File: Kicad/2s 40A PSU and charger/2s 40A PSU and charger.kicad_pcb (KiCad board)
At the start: 4 copper layers, 44.9 x 42 mm, 133 parts, among them J1 JST SH SM04B/Qwiic, J2 7 pin FPC 0.3mm Panasonic Y3b, J3 Conn_01x03, J4 Conn_01x03, J5 JST XH-S, Q1 PJA3430, Q2 PJA3430, Q3 Vishay sir404dp, Q4 PJA3430, Q5 PJA3430, Q7 Vishay sir404dp, SW1 KMR2, SW2 KMR2, U2 AP63203WU, U3 BQ76905RGRR, U4 BQ24780SRUYR, U5 ESP32-S3, U6 74HC595, Y1 40mhz, 10ppm

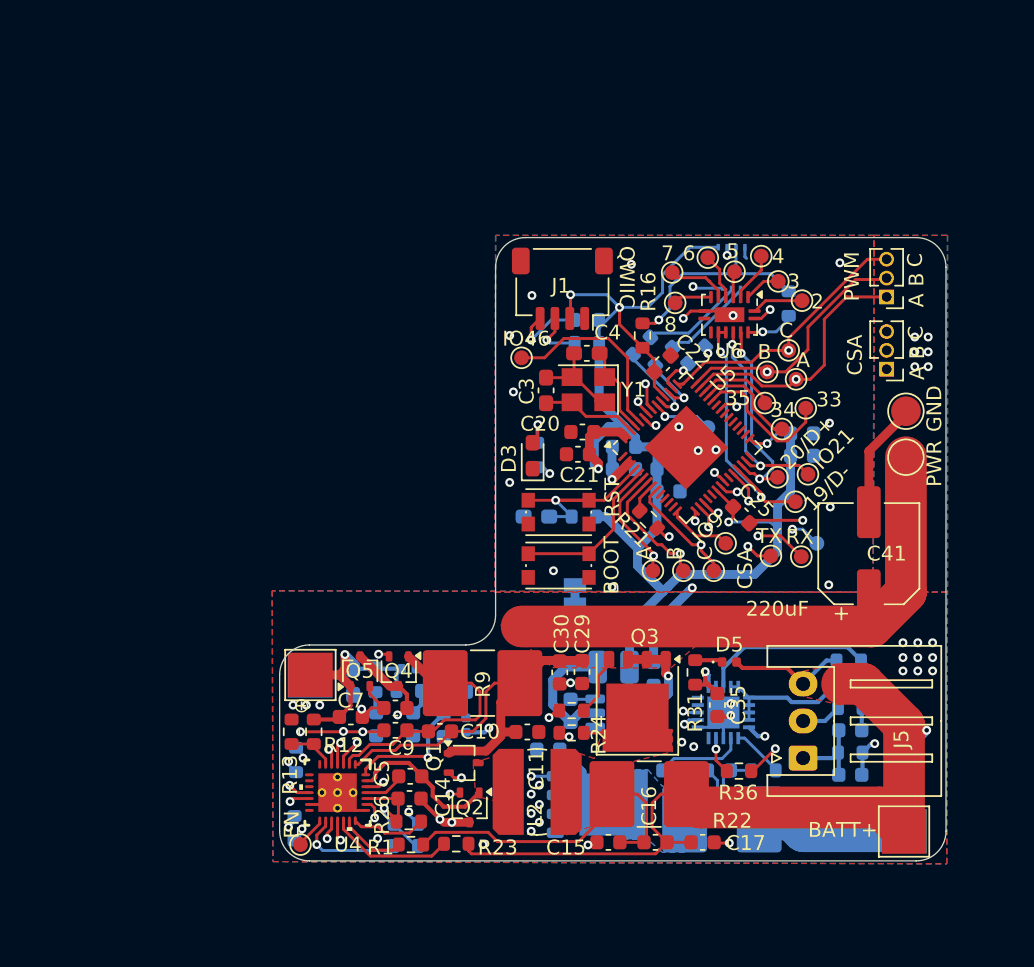
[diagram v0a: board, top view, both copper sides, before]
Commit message: Rearranged schematic hierarchy
It should be clearer than the original design from my testing board. I haven't changed any of the design things except getting the correct small transistor footprint (errata from before)
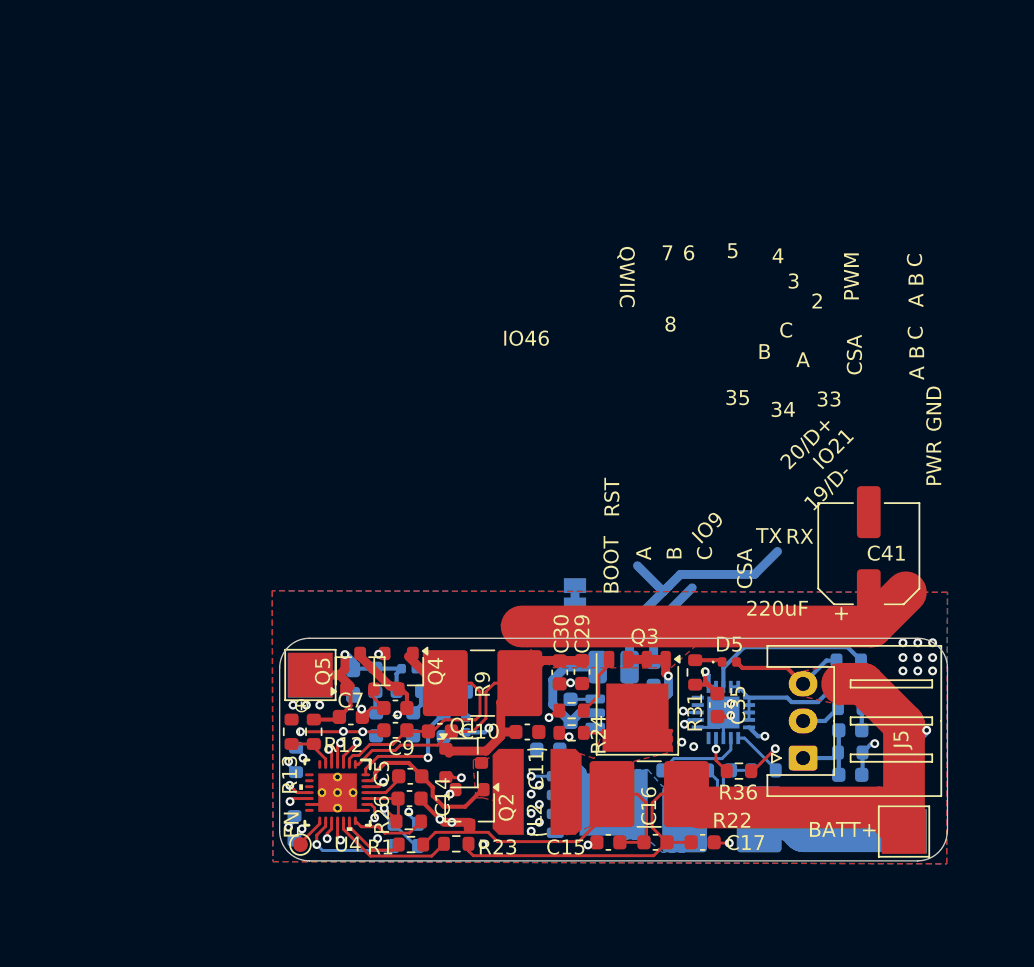
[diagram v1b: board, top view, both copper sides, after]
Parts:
- removed C1, C2, C21, C24: 1uF, Capacitor_SMD:C_0603_1608Metric
- removed C18: 1uF, Capacitor_SMD:C_0603_1608Metric_Pad1.08x0.95mm_HandSolder
- removed C19, C20, C22, C23, C25: 0.1uF, Capacitor_SMD:C_0603_1608Metric
- removed C26: 22uF, Capacitor_SMD:C_0603_1608Metric
- removed C3, C4: 16pF, Capacitor_SMD:C_0603_1608Metric_Pad1.08x0.95mm_HandSolder
- removed D3: Osram LT Q99G.01 green led, LED_SMD:LED_0603_1608Metric_Pad1.05x0.95mm_HandSolder
- removed FB1: 120ohm imp @100mhz, Inductor_SMD:L_0603_1608Metric
- removed H5: GND, TestPoint:TestPoint_Pad_D2.0mm
- removed H6: Power, TestPoint:TestPoint_Pad_D2.0mm
- removed J1: JST SH SM04B/Qwiic, Connector_JST:JST_SH_SM04B-SRSS-TB_1x04-1MP_P1.00mm_Horizontal
- removed J2: 7 pin FPC 0.3mm Panasonic Y3b, custom_Interface_HID:fpc_7pin_0.3mm_connector Panasonic
- removed J3, J4: Conn_01x03, Connector_PinHeader_1.27mm:PinHeader_1x03_P1.27mm_Vertical
- removed R14, R15, R16, R20: 10k, Resistor_SMD:R_0603_1608Metric
- removed R19: 80.6 ohm, Resistor_SMD:R_0603_1608Metric
- removed R21: 100k, Resistor_SMD:R_0603_1608Metric
- removed R3, R4, R5, R6: 33ohm, Resistor_SMD:R_0603_1608Metric
- removed SW1, SW2: KMR2, Button_Switch_SMD:SW_Push_1P1T_NO_CK_KMR2
- removed TP1, TP14, TP15: TestPoint, TestPoint:TestPoint_Pad_D1.0mm
- removed TP10, TP11, TP12, TP18, TP19, TP2, TP20, TP21, TP22, TP24, TP25, TP26, TP27, TP28, TP29, TP3, TP30, TP4, TP5, TP7, TP8, TP9: ~, TestPoint:TestPoint_Pad_D1.0mm
- removed U5: ESP32-S3, Package_DFN_QFN:QFN-56-1EP_7x7mm_P0.4mm_EP4x4mm
- removed U6: 74HC595, Package_DFN_QFN:DHVQFN-16-1EP_2.5x3.5mm_P0.5mm_EP1x2mm
- removed Y1: 40mhz, 10ppm, Crystal:Crystal_SMD_3225-4Pin_3.2x2.5mm
- Q1, Q2, Q4, Q5: footprint Package_TO_SOT_SMD:SOT-323_SC-70 -> Package_TO_SOT_SMD:SC-59
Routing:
- net VDD: track 108.8 -> 21.8 mm, vias 6 -> 0
- net /1CSA-A: track 36.1 -> 0.00 mm, vias 1 -> 0
- net /1CSA-B: track 35.7 -> 0.00 mm, vias 1 -> 0
- net /1CSA-C: track 33.3 -> 0.00 mm, vias 1 -> 0
- net /1A: track 28.2 -> 0.00 mm, vias 2 -> 0
- net /1B: track 26.3 -> 0.00 mm, vias 2 -> 0
- net /SCL1: track 78.5 -> 52.3 mm, vias 5 -> 3
- net /1C: track 25.6 -> 0.00 mm, vias 2 -> 0
- net /SDA1: track 72.3 -> 49.7 mm, vias 5 -> 3
- net /UART0_TX: track 19.9 -> 0.00 mm, vias 2 -> 0
- net Net-(U5-GPIO19/USB_D-): track 17.8 -> 0.00 mm, vias 2 -> 0
- net /UART0_RX: track 17.5 -> 0.00 mm, vias 2 -> 0
- net GND: track 22.6 -> 6.10 mm, vias 20 -> 0
- net /CS1: track 14.5 -> 0.00 mm, vias 1 -> 0
- net Net-(U5-GPIO21): track 14.4 -> 0.00 mm, vias 2 -> 0
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- removed copper zone on B.Cu, net GND
- removed copper zone on F.Cu, net GND
- removed copper zone on In1.Cu, net GND
- removed copper zone on In2.Cu, net GND
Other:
- board size 44.9 x 42 mm -> 45 x 15 mm
- rule pad_to_mask_clearance: 0 -> 0.05

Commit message: Reworked PSU to use CH32X035 and USB-PD
This will save a few bucks and will actually be a cooler solution than just a DC jack connected to some pads
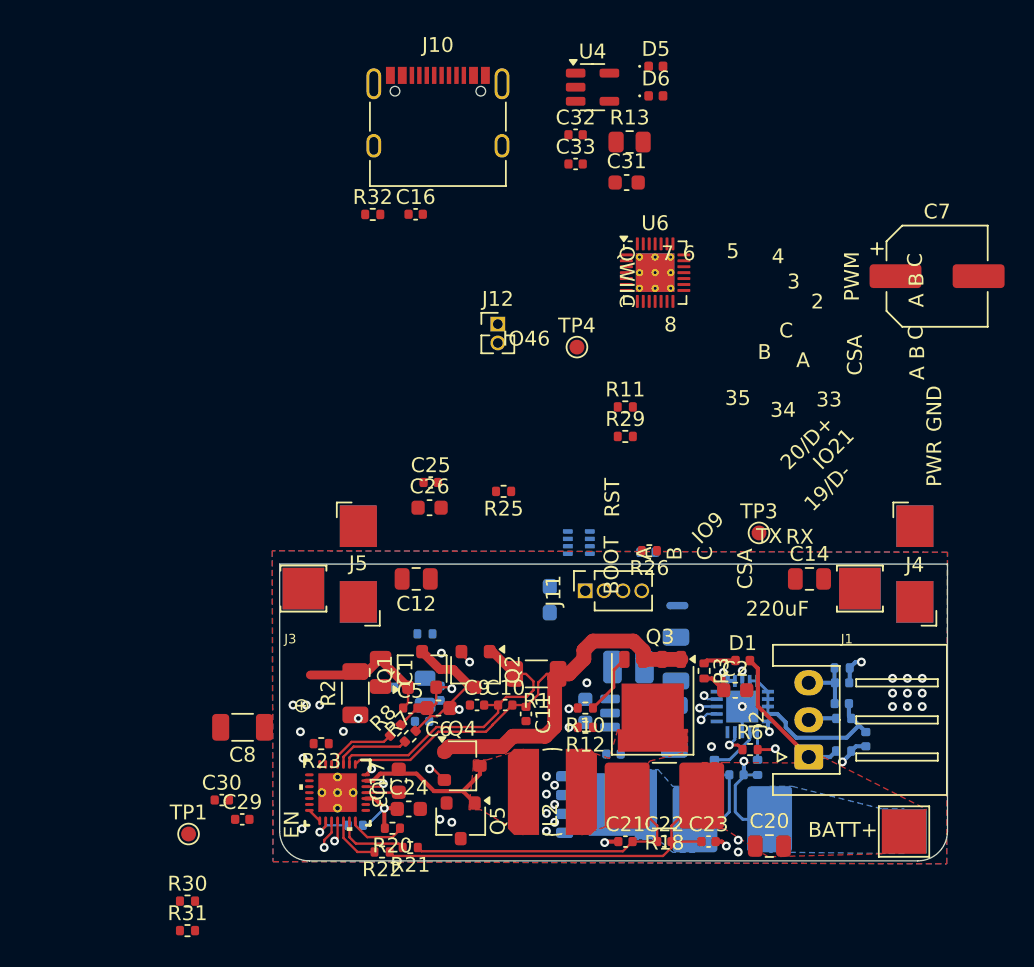
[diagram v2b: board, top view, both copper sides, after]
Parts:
- removed C34: 22nF, Capacitor_SMD:C_0603_1608Metric
- removed C35: 2.2uf, Capacitor_SMD:C_0603_1608Metric
- removed C36: 10uF, Capacitor_SMD:C_0603_1608Metric
- removed C37, C39: 220nF, Capacitor_SMD:C_0603_1608Metric
- removed C38: 0.1uF, Capacitor_SMD:C_0603_1608Metric
- removed C41: 220uF,APA0609221M016R, Capacitor_SMD:CP_Elec_6.3x9.9
- removed H3, H4: Pad, TestPoint:TestPoint_Pad_3.0x3.0mm
- removed L1: GND joiner, Jumper:SolderJumper-2_P1.3mm_Bridged_Pad1.0x1.5mm
- removed Q7: Vishay sir404dp, Package_DFN_QFN:PQFN-8-EP_6x5mm_P1.27mm_Generic
- removed R33, R34, R35: 10ohm, Resistor_SMD:R_0603_1608Metric
- removed R36: 5.1k, Resistor_SMD:R_0603_1608Metric
- removed TP6: ~, TestPoint:TestPoint_Pad_D1.0mm
- added C1: 10uF, 16v, Capacitor_SMD:C_0805_2012Metric, F.Cu at (114.9, 119.3)
- added C18: 220nF, 16v, Capacitor_SMD:C_0402_1005Metric, B.Cu at (146.0, 121.4)
- added C19: 220nF, 16v, Capacitor_SMD:C_0402_1005Metric, B.Cu at (146.0, 120.0)
- added C2: 2.2uf, 16v, Capacitor_SMD:C_0603_1608Metric, F.Cu at (138.8, 120.5)
- added C20: 10uF, 16v, Capacitor_SMD:C_0805_2012Metric, F.Cu at (141.1, 131.0)
- added C21: 0.1uF, 16v, Capacitor_SMD:C_0402_1005Metric, F.Cu at (131.4, 130.7)
- added C22: 0.1uF, 16v, Capacitor_SMD:C_0402_1005Metric, F.Cu at (134.0, 130.7)
- added C23: 0.1uF, 16v, Capacitor_SMD:C_0402_1005Metric, F.Cu at (137.0, 130.7)
- added C24: 2.2uf, Capacitor_SMD:C_0603_1608Metric, F.Cu at (116.8, 128.5)
- added C25: 0.1uF, Capacitor_SMD:C_0402_1005Metric, F.Cu at (118.3, 106.5)
- added C26: 4.7uF, Capacitor_SMD:C_0603_1608Metric, F.Cu at (118.2, 108.2)
- added C3: 0.1uF, 16v, Capacitor_SMD:C_0402_1005Metric, B.Cu at (138.9, 126.2)
- added C32: 0.1uF, 16v, Capacitor_SMD:C_0402_1005Metric, F.Cu at (128.0, 83.1)
- added C4: 0.1uF, Capacitor_SMD:C_0402_1005Metric, B.Cu at (130.6, 124.8)
- added D1: GSDH3005, Diode_SMD:D_0402_1005Metric, F.Cu at (139.3, 118.5)
- added D3: GSDH3005, Diode_SMD:D_0402_1005Metric, B.Cu at (118.9, 120.7)
- added D6: GSDH3005, Diode_SMD:D_0402_1005Metric, F.Cu at (133.4, 80.5)
- added J1: Keystone 3579, custom_Connector:Keystone_3579, F.Cu at (147.2, 113.7)
- added J10: USB_C_Receptacle_USB2.0_16P, Connector_USB:USB_C_Receptacle_XKB_U262-16XN-4BVC11, F.Cu at (118.8, 82.7)
- added J11: 1.27mm 4 pin socket, Connector_PinSocket_1.27mm:PinSocket_1x04_P1.27mm_Vertical, F.Cu at (128.7, 113.8)
- added J12: USB, Connector_PinHeader_1.27mm:PinHeader_1x02_P1.27mm_Vertical, F.Cu at (122.8, 95.8)
- added J2: JST XH-S, Connector_JST:JST_XH_S3B-XH-A_1x03_P2.50mm_Horizontal, F.Cu at (143.8, 125.0)
- added J3: Keystone 3579, custom_Connector:Keystone_3579, F.Cu at (109.7, 113.7)
- added J4: Keystone 3569, custom_Connector:Keystone_3569, F.Cu at (150.9, 112.0)
- added J6: Keystone 3579, custom_Connector:Keystone_3579, B.Cu at (147.2, 113.7)
- added J7: Keystone 3579, custom_Connector:Keystone_3579, B.Cu at (109.7, 113.7)
- added J8: Keystone 3569, custom_Connector:Keystone_3569, B.Cu at (150.9, 112.0)
- added J9: Keystone 3569, custom_Connector:Keystone_3569, B.Cu at (113.4, 112.0)
- added NT1: NetTie_2, NetTie:NetTie-2_SMD_Pad0.5mm, B.Cu at (134.9, 114.8)
- added Q6: Vishay sir404dp, or SiR500DP, Package_DFN_QFN:PQFN-8-EP_6x5mm_P1.27mm_Generic, B.Cu at (130.0, 128.2)
- added R14: 1mOhm, CS wshp2818, Resistor_SMD:R_2816_7142Metric, B.Cu at (138.6, 129.2)
- added R15: 10ohm, Resistor_SMD:R_0402_1005Metric, B.Cu at (146.1, 124.6)
- added R16: 10ohm, Resistor_SMD:R_0402_1005Metric, B.Cu at (146.1, 122.4)
- added R17: 10ohm, Resistor_SMD:R_0402_1005Metric, B.Cu at (146.0, 119.0)
- added R20: 10k, Resistor_SMD:R_0402_1005Metric, F.Cu at (115.7, 129.8)
- added R21: 10ohm, Resistor_SMD:R_0402_1005Metric, F.Cu at (116.9, 131.1)
- added R3: 100ohm, Resistor_SMD:R_0402_1005Metric, F.Cu at (136.7, 119.2)
- added R32: 100k, Resistor_SMD:R_0402_1005Metric, F.Cu at (114.4, 88.4)
- added R4: 100ohm, Resistor_SMD:R_0402_1005Metric, B.Cu at (140.3, 125.7)
- added R5: 100ohm, Resistor_SMD:R_0402_1005Metric, B.Cu at (137.4, 125.7)
- added R6: 5.1k, Resistor_SMD:R_0402_1005Metric, F.Cu at (139.8, 124.5)
- added TP1: SWC, TestPoint:TestPoint_Pad_D1.0mm, F.Cu at (102.0, 130.2)
- added TP3: ~, TestPoint:TestPoint_Pad_D1.0mm, F.Cu at (140.4, 109.9)
- added TP4: SWD, TestPoint:TestPoint_Pad_D1.0mm, F.Cu at (128.1, 97.4)
- added U1: BQ76905RGRR, BQ76905:VQFN20_RGR_TEX, B.Cu at (139.3, 121.6)
- added U5: THVD1420DRLR, Package_TO_SOT_SMD:SOT-583-8, B.Cu at (128.3, 110.5)
- added U6: CH32X035G8U6, Package_DFN_QFN:QFN-28-1EP_4x4mm_P0.4mm_EP2.6x2.6mm_ThermalVias, F.Cu at (133.4, 92.4)
- C10, C11, C9: value 0.1uF -> 0.1uF, 16v; footprint Capacitor_SMD:C_0603_1608Metric -> Capacitor_SMD:C_0402_1005Metric
- C12: value 1uf -> 10uF, 16v; footprint Capacitor_SMD:C_0603_1608Metric -> Capacitor_SMD:C_0805_2012Metric; moved to F.Cu
- C13: value 10uF, 16v -> 220nF, 16v; footprint Capacitor_SMD:C_0603_1608Metric_Pad1.08x0.95mm_HandSolder -> Capacitor_SMD:C_0402_1005Metric
- C14: value 2.2uf -> 10uF, 16v; footprint Capacitor_SMD:C_0603_1608Metric -> Capacitor_SMD:C_0805_2012Metric
- C15: value 0.1uF -> 1uf, 16v; footprint Capacitor_SMD:C_0603_1608Metric -> Capacitor_SMD:C_0402_1005Metric; moved to B.Cu
- C16: value 0.1uF -> 100nF; footprint Capacitor_SMD:C_0603_1608Metric -> Capacitor_SMD:C_0402_1005Metric
- C17: value 0.1uF -> 47nF, 16v
- C27, C28: value 22uf -> 22uf, 16v CL31A226MOCLNN; footprint Capacitor_SMD:C_0603_1608Metric -> Capacitor_SMD:C_1206_3216Metric
- C29, C30: value 10uF -> 100pF; footprint Capacitor_SMD:C_0603_1608Metric -> Capacitor_SMD:C_0402_1005Metric
- C31: value 2.2uf -> 10uF, 16v; moved to F.Cu
- C33: value 0.1uF -> 2.2uF, 10v; footprint Capacitor_SMD:C_0603_1608Metric -> Capacitor_SMD:C_0402_1005Metric; moved to F.Cu
- C5: value 47nF -> 1nF; footprint Capacitor_SMD:C_0603_1608Metric -> Capacitor_SMD:C_0402_1005Metric
- C6: value 2.2uf -> 47nf; moved to F.Cu
- C7: value 1nF -> 220uF,APA0609221M016R; footprint Capacitor_SMD:C_0603_1608Metric -> Capacitor_SMD:CP_Elec_6.3x9.9
- C8: value 47nf -> 2.2uf, 16v; footprint Capacitor_SMD:C_0603_1608Metric -> Capacitor_SMD:C_1206_3216Metric
- D4: value GSDH3005 -> Osram LT Q99G.01 green led; footprint Diode_SMD:D_0402_1005Metric -> LED_SMD:LED_0603_1608Metric_Pad1.05x0.95mm_HandSolder
- J5: value JST XH-S -> Keystone 3569; footprint Connector_JST:JST_XH_S3B-XH-A_1x03_P2.50mm_Horizontal -> custom_Connector:Keystone_3569
- L2: value 5.6uH Bourns SDE0604A -> 6.8uH HPC HPC5040NF-6R8M
- L3: value 4.7uH, MAMK2520T4R7M -> 2.2uH, WIP322512A-2R2MLDG
- Q3: value Vishay sir404dp -> Vishay sir404dp, or SiR500DP
- R1: value 10ohm -> 10mOhm LVT12R0100FER; footprint Resistor_SMD:R_0603_1608Metric -> Resistor_SMD:R_1206_3216Metric
- R10: value 10k -> 4.02kohm; footprint Resistor_SMD:R_0603_1608Metric -> Resistor_SMD:R_0402_1005Metric; moved to F.Cu
- R11: value 2ohm -> 10k; footprint Resistor_SMD:R_0603_1608Metric -> Resistor_SMD:R_0402_1005Metric; moved to F.Cu
- R12: value 866k -> 10ohm; footprint Resistor_SMD:R_0603_1608Metric -> Resistor_SMD:R_0402_1005Metric
- R13: value 133k -> 10 ohm; footprint Resistor_SMD:R_0603_1608Metric -> Resistor_SMD:R_0805_2012Metric
- R18: value 10k -> 5mOhm, CS wshp2818; footprint Resistor_SMD:R_0603_1608Metric -> Resistor_SMD:R_2816_7142Metric; moved to F.Cu
- R2: value 4.02k -> 2ohm; footprint Resistor_SMD:R_0603_1608Metric -> Resistor_SMD:R_1206_3216Metric; moved to F.Cu
- R22: value 5mOhm, CS wshp2818 -> 10ohm; footprint Resistor_SMD:R_2816_7142Metric -> Resistor_SMD:R_0402_1005Metric
- R23: value 10ohm -> 10k; footprint Resistor_SMD:R_0603_1608Metric -> Resistor_SMD:R_0402_1005Metric
- R24: value 10ohm -> 10k; footprint Resistor_SMD:R_0603_1608Metric -> Resistor_SMD:R_0402_1005Metric; moved to B.Cu
- R25: value 4.02kohm -> 80.6 ohm; footprint Resistor_SMD:R_0603_1608Metric -> Resistor_SMD:R_0402_1005Metric
- R26: value 10k -> 120 ohm; footprint Resistor_SMD:R_0603_1608Metric -> Resistor_SMD:R_0402_1005Metric
- R27: value 1mOhm, CS wshp2818 -> 120 ohm; footprint Resistor_SMD:R_2816_7142Metric -> Resistor_SMD:R_0402_1005Metric
- R28: value 2ohm -> 120 ohm; footprint Resistor_SMD:R_0603_1608Metric -> Resistor_SMD:R_0402_1005Metric
- R29: value 100ohm -> 10k; footprint Resistor_SMD:R_0603_1608Metric -> Resistor_SMD:R_0402_1005Metric; moved to F.Cu
- R30: value 100ohm -> 866k; footprint Resistor_SMD:R_0603_1608Metric -> Resistor_SMD:R_0402_1005Metric; moved to F.Cu
- R31: value 10k -> 866k; footprint Resistor_SMD:R_0603_1608Metric -> Resistor_SMD:R_0402_1005Metric
- R7: footprint Resistor_SMD:R_0603_1608Metric -> Resistor_SMD:R_0402_1005Metric; moved to F.Cu
- R8: value 10k -> 4.02k; footprint Resistor_SMD:R_0603_1608Metric -> Resistor_SMD:R_0402_1005Metric; moved to F.Cu
- R9: value 5mOhm CS wshp2818 -> 10 ohm; footprint Resistor_SMD:R_2816_7142Metric -> Resistor_SMD:R_0805_2012Metric; moved to B.Cu
- U3: value BQ76905RGRR -> BQ24780SRUYR; footprint BQ76905:VQFN20_RGR_TEX -> BQ24780:RUY0028A; moved to F.Cu
- U4: value BQ24780SRUYR -> LP2981-3.3; footprint BQ24780:RUY0028A -> Package_TO_SOT_SMD:SOT-23-5
- moved U4 50.5 mm to (129.2, 79.9), turned to 0 degrees
- moved C7 49.4 mm to (152.4, 92.6)
- moved R13 45.8 mm to (131.7, 83.6), turned to 0 degrees
- moved C16 45.3 mm to (117.3, 88.4)
- moved C33 42.0 mm to (128.0, 85.0), turned to 0 degrees
- moved D5 40.4 mm to (133.4, 78.5)
- moved C31 39.2 mm to (131.5, 86.3), turned to 0 degrees
- moved R31 38.4 mm to (101.9, 136.7), turned to 0 degrees
- moved C13 34.8 mm to (147.6, 123.8), turned to 90 degrees
- moved R30 34.0 mm to (101.9, 134.7)
- moved J5 32.7 mm to (113.4, 112.0), turned to 180 degrees
- moved C14 30.7 mm to (143.8, 113.0)
- moved U3 26.6 mm to (112.0, 127.4), turned to -90 degrees
- moved C29 25.0 mm to (105.6, 129.2), turned to 0 degrees
- moved R11 24.9 mm to (131.4, 101.4), turned to 0 degrees
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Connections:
- net VDD renamed /Connectors/3.3v
- C10 pad 1: Net-(Q4-D) -> Net-(Q2-D)
- C10 pad 2: /MOTORPWR -> /Battery Charger/MOTORPWR
- C11 pad 1: /MOTORPWR -> /Battery Charger/MOTORPWR
- C11 pad 2: GNDPWR -> GND
- C12 pad 1: Net-(U4-VCC) -> GNDPWR
- C12 pad 2: GNDPWR -> /Battery Charger/MOTORPWR
- C13 pad 1: /PSU/IN -> /Battery Balancer/Up
- C13 pad 2: GNDPWR -> /Battery Balancer/Mid
- C14 pad 1: /PSU/REGN -> GNDPWR
- C14 pad 2: GNDPWR -> /Battery Charger/MOTORPWR
- C15 pad 1: GNDPWR -> Net-(U3-VCC)
- C15 pad 2: Net-(Q3-S) -> GND
- C16 pad 1: Net-(Q3-S) -> GNDPWR
- C16 pad 2: /PSU/BATT+ -> Net-(J10-SHIELD)
- C17 pad 1: /PSU/BATT+ -> Net-(U3-BTST)
- C17 pad 2: GNDPWR -> Net-(Q4-S)
- C28 pad 1: /MOTORPWR -> /Battery Charger/MOTORPWR
- C29 pad 1: GNDPWR -> /Battery Charger/Charger IADP
- C29 pad 2: /MOTORPWR -> GND
- C30 pad 1: GNDPWR -> /Battery Charger/Charger IDCHG
- C30 pad 2: /MOTORPWR -> GND
- C31 pad 1: Net-(C31-Pad1) -> Net-(U4-ON/~{OFF})
- C33 pad 1: /PSU/BATT- -> /MCU/3.3v
- C33 pad 2: Net-(Q7-S) -> GNDPWR
- C5 pad 1: Net-(U4-BTST) -> /Battery Charger/IN
- C5 pad 2: Net-(Q1-S) -> Net-(Q1-G)
- C6 pad 1: Net-(C6-Pad1) -> Net-(Q1-S)
- C6 pad 2: GNDPWR -> Net-(Q1-G)
- C7 pad 1: /PSU/IN -> /Battery Charger/MOTORPWR
- C7 pad 2: Net-(Q4-G) -> GNDPWR
- C8 pad 1: Net-(Q4-S) -> Net-(C8-Pad1)
- C8 pad 2: Net-(Q4-G) -> GNDPWR
- C9 pad 1: GNDPWR -> GND
- C9 pad 2: Net-(Q4-D) -> Net-(Q2-D)
- D2 pad 2: /PSU/IN -> /Battery Charger/IN
- D4 pad 1: Net-(D2-K) -> GND
- D4 pad 2: /PSU/BATT+ -> Net-(D4-A)
- D5 pad 2: /PSU/BATT+ -> /Battery Charger/IN
- H1 pad 1: /PSU/BATT+ -> /Battery Balancer/BAT+
- H2 pad 1: /PSU/BATT- -> /Battery Balancer/BAT-
- J5 pad 1: Net-(J5-Pin_1) -> /Battery Charger/MOTORPWR
- L2 pad 1: Net-(Q1-S) -> Net-(Q4-S)
- Q1 pad 1: /MOTORPWR -> /Battery Charger/IN
- Q2 pad 1: Net-(Q1-S) -> Net-(Q2-D)
- Q2 pad 2: Net-(Q2-G) -> Net-(Q1-G)
- Q2 pad 3: GNDPWR -> Net-(Q1-S)
- Q3 pad 1: /MOTORPWR -> /Battery Charger/MOTORPWR
- Q3 pad 2: /MOTORPWR -> /Battery Charger/MOTORPWR
- Q3 pad 3: /MOTORPWR -> /Battery Charger/MOTORPWR
- Q4 pad 1: Net-(Q4-D) -> /Battery Charger/MOTORPWR
- Q5 pad 1: /PSU/IN -> Net-(Q4-S)
- Q5 pad 2: Net-(Q4-G) -> Net-(Q5-G)
- Q5 pad 3: Net-(Q4-S) -> GNDPWR
- R1 pad 1: Net-(Q3-S) -> /Battery Charger/MOTORPWR
- R1 pad 2: Net-(U4-SRP) -> Net-(Q2-D)
- R10 pad 1: Net-(U4-VCC) -> Net-(Q3-G)
- R10 pad 2: Net-(D2-K) -> Net-(U3-BATDRV)
- R11 pad 1: Net-(C6-Pad1) -> /SDA
- R11 pad 2: /PSU/IN -> /MCU/3.3v
- R12 pad 1: Net-(U4-ACDET) -> Net-(Q3-S)
- R12 pad 2: /PSU/IN -> Net-(U3-BATSRC)
- R13 pad 1: GNDPWR -> Net-(U4-ON/~{OFF})
- R13 pad 2: Net-(U4-ACDET) -> Net-(D5-K)
- R18 pad 1: /PSU/REGN -> /Battery Balancer/BAT+
- R18 pad 2: Net-(U4-TB_STAT_N) -> Net-(Q3-S)
- R2 pad 1: Net-(U4-ACDRV) -> Net-(C8-Pad1)
- R2 pad 2: Net-(Q4-G) -> /Battery Charger/IN
- R22 pad 1: /PSU/BATT+ -> /Battery Balancer/BAT+
- R22 pad 2: Net-(Q3-S) -> Net-(U3-SRN)
- R23 pad 1: /PSU/BATT+ -> /Battery Charger/REGN
- R23 pad 2: Net-(U4-SRN) -> Net-(U3-ACOK)
- R24 pad 1: Net-(Q3-S) -> /Battery Charger/REGN
- R24 pad 2: Net-(U4-BATSRC) -> Net-(U3-TB_STAT_N)
- R25 pad 1: Net-(Q3-G) -> /MCU/LED
- R25 pad 2: Net-(U4-BATDRV) -> Net-(D4-A)
- R26 pad 1: Net-(U4-ILIM) -> /Connectors/RS485-
- R26 pad 2: /PSU/REGN -> GND
- R27 pad 1: Net-(Q7-S) -> /Connectors/RS485-
- R27 pad 2: /PSU/BATT- -> /Connectors/RS485+
- R28 pad 1: /PSU/IN -> /MCU/3.3v
- R28 pad 2: Net-(C31-Pad1) -> /Connectors/RS485+
- R29 pad 1: Net-(U3-SRP) -> /SCL
- R29 pad 2: /PSU/BATT- -> /MCU/3.3v
- R30 pad 1: Net-(U3-SRN) -> Net-(U3-CMPIN)
- R30 pad 2: Net-(Q7-S) -> /Battery Balancer/BAT+
- R31 pad 1: Net-(D5-K) -> GNDPWR
- R31 pad 2: Net-(U3-BAT) -> Net-(U3-CMPIN)
- R7 pad 1: Net-(U4-CMSRC) -> Net-(U3-CMSRC)
- R7 pad 2: Net-(Q4-S) -> Net-(Q1-S)
- R8 pad 1: /PSU/REGN -> Net-(U3-ACDRV)
- R8 pad 2: Net-(U4-ACOK) -> Net-(Q1-G)
- R9 pad 1: /MOTORPWR -> Net-(U3-VCC)
- R9 pad 2: Net-(Q4-D) -> Net-(D2-K)
- U2 pad 2: /MOTORPWR -> /Battery Charger/MOTORPWR
- U2 pad 3: /MOTORPWR -> /Battery Charger/MOTORPWR
- U3 pad 1: /PSU/mid -> /Battery Charger/MOTORPWR
- U3 pad 10: unconnected-(U3-CHG-Pad10) -> /Battery Charger/Charger PROCHOT
- U3 pad 11: GNDPWR -> /SDA
- U3 pad 12: /SCL1 -> /SCL
- U3 pad 13: /SDA1 -> Net-(U3-CMPIN)
- U3 pad 14: unconnected-(U3-ALERT-Pad14) -> Net-(U3-BATPRES_N)
- U3 pad 15: unconnected-(U3-REGOUT-Pad15) -> Net-(U3-BATPRES_N)
- U3 pad 16: Net-(U3-BAT) -> Net-(U3-TB_STAT_N)
- U3 pad 17: Net-(U3-BAT) -> Net-(U3-BATSRC)
- U3 pad 18: /PSU/Up -> Net-(U3-BATDRV)
- U3 pad 19: /PSU/mid -> Net-(U3-SRN)
- U3 pad 2: /PSU/mid -> Net-(Q2-D)
- U3 pad 20: /PSU/mid -> Net-(U3-SRP)
- U3 pad 21: GNDPWR -> Net-(U3-ILIM)
- U3 pad 3: /PSU/mid -> Net-(U3-CMSRC)
- U3 pad 4: /PSU/mid -> Net-(U3-ACDRV)
- U3 pad 5: /PSU/Low -> Net-(U3-ACOK)
- U3 pad 6: Net-(U3-SRP) -> /Battery Charger/PWRON
- U3 pad 7: Net-(U3-SRN) -> /Battery Charger/Charger IADP
- U3 pad 8: GNDPWR -> /Battery Charger/Charger IDCHG
- U3 pad 9: Net-(U3-DSG) -> unconnected-(U3-PMON-Pad9)
- U4 pad 1: /MOTORPWR -> Net-(U4-ON/~{OFF})
- U4 pad 2: Net-(Q4-D) -> GNDPWR
- U4 pad 3: Net-(U4-CMSRC) -> Net-(U4-ON/~{OFF})
- U4 pad 4: Net-(U4-ACDRV) -> unconnected-(U4-BP-Pad4)
- U4 pad 5: Net-(U4-ACOK) -> /MCU/3.3v
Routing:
- net /PSU/BATT+: track 93.0 -> 0.00 mm, vias 2 -> 0
- net /MOTORPWR: track 64.7 -> 0.00 mm, vias 1 -> 0
- net /SCL1: track 52.3 -> 0.00 mm, vias 3 -> 0
- net /SDA1: track 49.7 -> 0.00 mm, vias 3 -> 0
- net /Battery Charger/MOTORPWR: track 0.00 -> 39.0 mm
- net /Battery Balancer/BAT+: track 0.00 -> 36.0 mm
- net /Battery Balancer/BAT-: track 0.00 -> 27.0 mm, vias 0 -> 1
- net Net-(U3-BATSRC): track 0.00 -> 23.6 mm, vias 0 -> 2
- net Net-(U4-BATSRC): track 23.2 -> 0.00 mm, vias 2 -> 0
- net /Connectors/3.3v: track 21.8 -> 0.00 mm
- net Net-(U3-BATDRV): track 0.00 -> 21.5 mm, vias 0 -> 2
- net Net-(Q7-G): track 21.1 -> 0.00 mm, vias 2 -> 0
- net Net-(U4-BATDRV): track 20.8 -> 0.00 mm, vias 2 -> 0
- net Net-(Q2-D): track 0.00 -> 20.4 mm
- net GNDPWR: track 21.4 -> 1.80 mm, vias 30 -> 29
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- added copper zone on B.Cu, net (none)
- added copper zone on F.Cu, net /Battery Balancer/BAT+
- added copper zone on B.Cu, net /Battery Balancer/BAT-
- added copper zone on F.Cu, net Net-(Q4-S)
- removed copper zone on F.Cu, net /MOTORPWR
- removed copper zone on F.Cu, net /PSU/BATT+
- removed copper zone on F.Cu, net Net-(Q1-S)
- removed copper zone on B.Cu, net Net-(Q7-S)
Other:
- board size 45 x 15 mm -> 45 x 20 mm

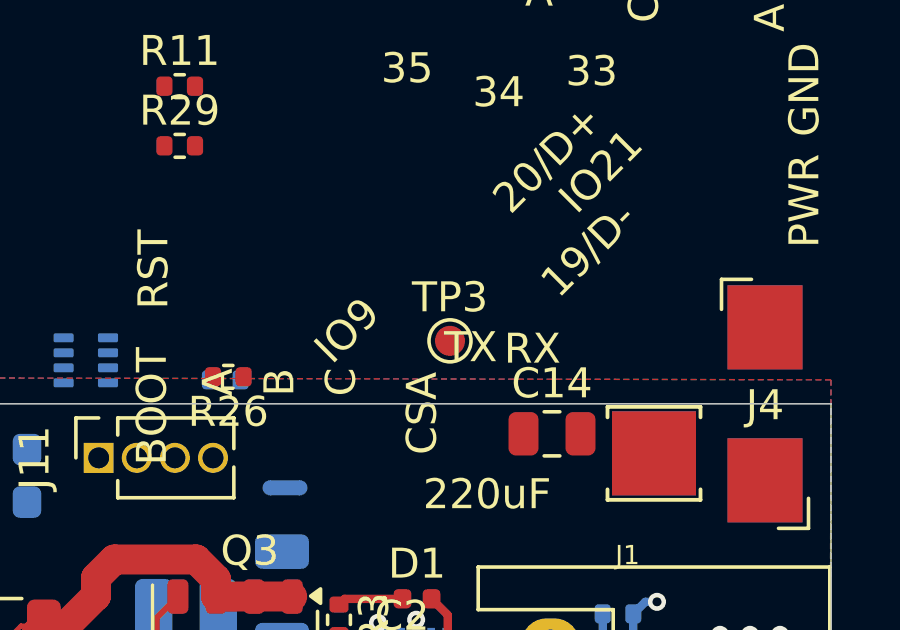
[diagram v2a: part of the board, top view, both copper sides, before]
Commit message: Improved schematic formatting and visuals
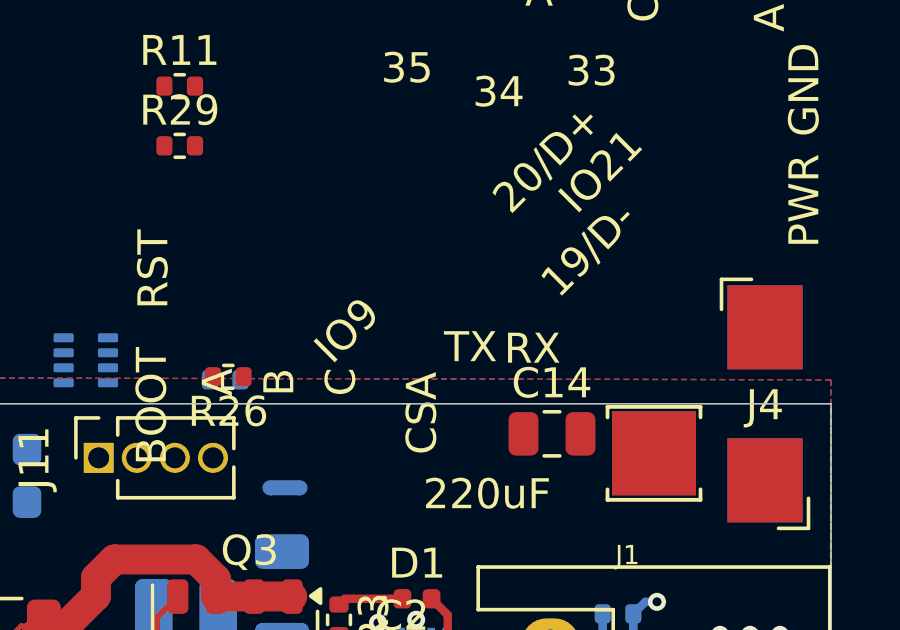
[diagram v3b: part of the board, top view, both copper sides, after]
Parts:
- removed TP3: ~, TestPoint:TestPoint_Pad_D1.0mm
- H1: value Pad -> Bat+
- H2: value Pad -> Bat-
- J2: value JST XH-S -> JST XH-S Balance Plug
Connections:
- R11 pad 1: /SDA -> /SCL
- R29 pad 1: /SCL -> /SDA
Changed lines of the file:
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@@
 		)
 	)
-	(footprint "TestPoint:TestPoint_Pad_D1.0mm"
-		(layer "F.Cu")
-		(at 140.4 109.9)
-		(descr "SMD pad as test Point, diameter 1.0mm")
-		(tags "test point SMD pad")
-		(property "Reference" "TP3"
-			(at 0 -1.448 0)
-			(layer "F.SilkS")
-			(effects
-				(font
-					(size 1 1)
-					(thickness 0.15)
-				)
-			)
-		)
-		(property "Value" "~"
-			(at 0 1.55 0)
-			(layer "F.Fab")
-			(effects
-				(font
-					(size 1 1)
-					(thickness 0.15)
-				)
-			)
-		)
-		(property "Footprint" "TestPoint:TestPoint_Pad_D1.0mm"
-			(at 0 0 0)
-			(unlocked yes)
-			(layer "F.Fab")
-			(hide yes)
-			(effects
-				(font
-					(size 1.27 1.27)
-					(thickness 0.15)
-				)
-			)
-		)
-		(property "Datasheet" ""
-			(at 0 0 0)
-			(unlocked yes)
-			(layer "F.Fab")
-			(hide yes)
-			(effects
-				(font
-					(size 1.27 1.27)
-					(thickness 0.15)
-				)
-			)
-		)
-		(property "Description" "test point"
-			(at 0 0 0)
-			(unlocked yes)
-			(layer "F.Fab")
-			(hide yes)
-			(effects
-				(font
-					(size 1.27 1.27)
-					(thickness 0.15)
-				)
-			)
-		)
-		(property ki_fp_filters "Pin* Test*")
-		(sheetname "MCU")
-		(sheetfile "MCU.kicad_sch")
-		(attr exclude_from_pos_files exclude_from_bom)
-		(fp_circle
-			(center 0 0)
-			(end 0 0.7)
-			(stroke
-				(width 0.12)
-				(type solid)
-			)
-			(fill none)
-			(layer "F.SilkS")
-		)
-		(fp_circle
-			(center 0 0)
-			(end 1 0)
-			(stroke
-				(width 0.05)
-				(type solid)
-			)
-			(fill none)
-			(layer "F.CrtYd")
-		)
-		(fp_text user "${REFERENCE}"
-			(at 0 -1.45 0)
-			(layer "F.Fab")
-			(effects
-				(font
-					(size 1 1)
-					(thickness 0.15)
-				)
-			)
-		)
-		(pad "1" smd circle
-			(at 0 0)
-			(size 1 1)
-			(layers "F.Cu" "F.Mask")
-			(net 64 "/Connectors/D+")
-			(pinfunction "1")
-			(pintype "passive")
-		)
-	)
 	(footprint "Capacitor_SMD:C_0402_1005Metric"
 		(layer "F.Cu")
@@
 			)
 		)
-		(property "Value" "JST XH-S"
+		(property "Value" "JST XH-S Balance Plug"
 			(at 2.5 10.4 90)
 			(layer "F.Fab")
@@
 			(layers "F.Cu" "F.Paste" "F.Mask")
 			(roundrect_rratio 0.25)
-			(net 51 "/SCL")
+			(net 54 "/SDA")
 			(pintype "passive")
 		)
@@
 			)
 		)
-		(property "Value" "Pad"
+		(property "Value" "Bat+"
 			(at 0 2.55 0)
 			(layer "F.Fab")
@@
 			(layers "F.Cu" "F.Paste" "F.Mask")
 			(roundrect_rratio 0.25)
-			(net 54 "/SDA")
+			(net 51 "/SCL")
 			(pintype "passive")
 		)
@@
 			)
 		)
-		(property "Value" "Pad"
+		(property "Value" "Bat-"
 			(at 0 -2.55 0)
 			(layer "B.Fab")

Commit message: Changed onboard mcu regulator
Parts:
- U4: value LP2981-3.3 -> TLV709A33DBVR
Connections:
- C31 pad 1: Net-(U4-ON/~{OFF}) -> Net-(U4-VIN)
- C32 pad 1: Net-(U4-ON/~{OFF}) -> Net-(U4-VIN)
- R13 pad 1: Net-(U4-ON/~{OFF}) -> Net-(U4-VIN)
- U4 pad 1: Net-(U4-ON/~{OFF}) -> Net-(U4-VIN)
- U4 pad 3: Net-(U4-ON/~{OFF}) -> unconnected-(U4-ON/~{OFF}-Pad3)
